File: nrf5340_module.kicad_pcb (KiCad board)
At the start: 4 copper layers, 18 x 40 mm, 42 parts, among them J1 U.FL_A-1JB, U1 nrf5340, Y1 32.768kHz, Y2 32MHz

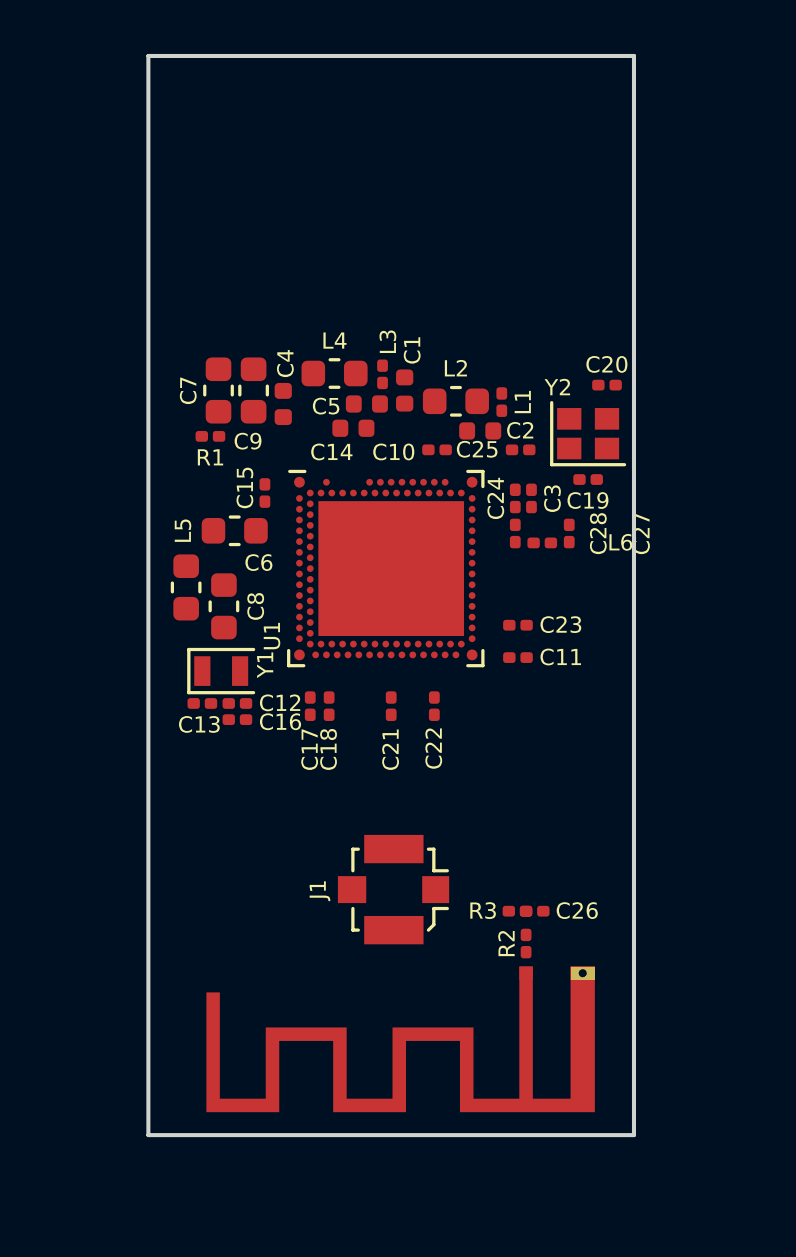
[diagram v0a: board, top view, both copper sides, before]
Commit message: first rev pcb without impedance matching
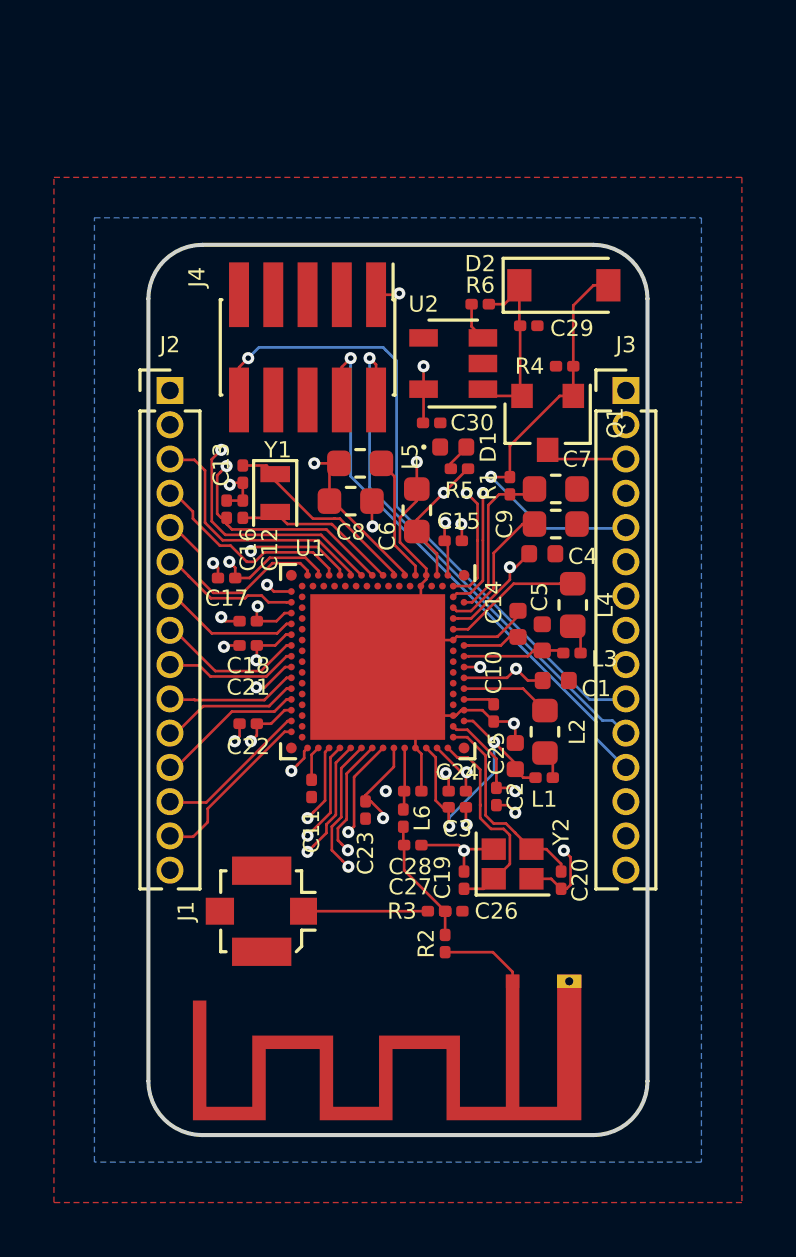
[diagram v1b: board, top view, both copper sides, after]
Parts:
- added C29: 10uF, Capacitor_SMD:C_0201_0603Metric, F.Cu at (234.1, 130.0)
- added C30: 10uF, Capacitor_SMD:C_0201_0603Metric, F.Cu at (230.5, 133.6)
- added D1: LED, LED_SMD:LED_0402_1005Metric, F.Cu at (231.3, 134.5)
- added D2: MBR120, Diode_SMD:D_SOD-123, F.Cu at (235.4, 128.5)
- added J2: Conn_01x15, Connector_PinHeader_1.27mm:PinHeader_1x15_P1.27mm_Vertical, F.Cu at (220.8, 132.4)
- added J3: Conn_01x15, Connector_PinHeader_1.27mm:PinHeader_1x15_P1.27mm_Vertical, F.Cu at (237.7, 132.4)
- added J4: Conn_ARM_JTAG_SWD_10, Connector_PinHeader_1.27mm:PinHeader_2x05_P1.27mm_Vertical_SMD, F.Cu at (225.9, 130.8)
- added Q1: Q_PMOS_GSD, Package_TO_SOT_SMD:SOT-23, F.Cu at (234.8, 133.6)
- added R4: 100k, Resistor_SMD:R_0201_0603Metric, F.Cu at (235.4, 131.5)
- added R5: 68R, Resistor_SMD:R_0201_0603Metric, F.Cu at (231.5, 135.3)
- added R6: 100k, Resistor_SMD:R_0201_0603Metric, F.Cu at (232.3, 129.2)
- added U2: AP2112K-3.3, Package_TO_SOT_SMD:SOT-23-5, F.Cu at (231.3, 131.4)
- moved C20 18.4 mm to (235.3, 150.6), turned to 90 degrees
- moved Y2 16.2 mm to (233.5, 149.9)
- moved C19 15.5 mm to (231.7, 150.6), turned to 270 degrees
- moved L1 14.0 mm to (234.7, 146.8), turned to 0 degrees
- moved C7 13.0 mm to (235.1, 136.1), turned to 0 degrees
- moved C27 12.9 mm to (229.8, 149.2), turned to 180 degrees
- moved C25 12.9 mm to (232.9, 147.4), turned to 90 degrees
- moved L2 12.7 mm to (234.7, 145.1), turned to 90 degrees
- moved L3 12.5 mm to (235.7, 142.1), turned to 0 degrees
- moved L4 12.3 mm to (235.7, 140.3), turned to 90 degrees
- moved C9 12.2 mm to (235.1, 137.3), turned to 0 degrees
- moved C1 12.1 mm to (235.1, 143.2), turned to 180 degrees
- moved C2 12.1 mm to (233.6, 145.9), turned to 90 degrees
- moved C3 11.8 mm to (231.4, 147.8), turned to 0 degrees
- moved L6 11.4 mm to (229.4, 148.2), turned to 90 degrees
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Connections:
- net P0.04 renamed Net-(U1-PadV2)
- net P0.05 renamed Net-(U1-PadY2)
- net P0.06 renamed Net-(U1-PadAB2)
- net P0.07 renamed Net-(U1-PadAD2)
- net P0.08 renamed Net-(U1-PadAH2)
- net P0.10 renamed Net-(U1-PadAK2)
- net P0.11 renamed Net-(U1-PadAK4)
- net P0.12 renamed Net-(U1-PadAK6)
- net P0.14 renamed Net-(U1-PadAK8)
- net P0.15 renamed Net-(U1-PadAK10)
- net P0.17 renamed Net-(U1-PadAK12)
- net P0.18 renamed Net-(U1-PadAK14)
- net P0.20 renamed Net-(U1-PadAK16)
- net P0.22 renamed Net-(U1-PadAK18)
- net P0.23 renamed Net-(U1-PadAK20)
- net P0.25 renamed Net-(U1-PadAK28)
- net P0.27 renamed Net-(U1-PadAK30)
- net P0.30 renamed Net-(U1-PadB24)
- net P0.31 renamed Net-(U1-PadB22)
- net P1.00 renamed Net-(U1-PadM2)
- net P1.01 renamed Net-(U1-PadP2)
- net P1.03 renamed Net-(U1-PadAF2)
- net P1.05 renamed Net-(U1-PadAK22)
- net P1.07 renamed Net-(U1-PadAK24)
- net P1.09 renamed Net-(U1-PadAK26)
- net P1.11 renamed Net-(U1-PadB20)
- net P1.12 renamed Net-(U1-PadB18)
- net P1.14 renamed Net-(U1-PadB16)
- net P1.15 renamed Net-(U1-PadB14)
- U1 pad B30: Net-(C12-Pad2) -> Net-(C20-Pad2)
- U1 pad C31: Net-(C13-Pad1) -> Net-(C19-Pad2)
- U1 pad K2: (no net) -> Net-(U1-PadK2)
- U1 pad N1: Net-(C19-Pad2) -> Net-(C13-Pad1)
- U1 pad R1: Net-(C20-Pad2) -> Net-(C12-Pad2)
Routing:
- net VDD_nRF: track 0.00 -> 60.5 mm, vias 0 -> 19
- net nRESET: track 0.00 -> 42.4 mm, vias 0 -> 2
- net GND: track 0.00 -> 41.9 mm, vias 0 -> 15
- net SWDCLK: track 0.00 -> 40.4 mm, vias 0 -> 2
- net SWDIO: track 0.00 -> 39.2 mm, vias 0 -> 2
- net P0.02: track 0.00 -> 24.9 mm, vias 0 -> 1
- net P0.28: track 0.00 -> 17.3 mm, vias 0 -> 1
- net P1.10: track 0.00 -> 16.2 mm, vias 0 -> 1
- net VBUS: track 0.00 -> 15.7 mm, vias 0 -> 1
- net P0.29: track 0.00 -> 15.0 mm, vias 0 -> 1
- net D+: track 0.00 -> 11.8 mm, vias 0 -> 1
- net D-: track 0.00 -> 11.0 mm, vias 0 -> 1
- net Net-(C2-Pad1): track 0.00 -> 10.8 mm, vias 0 -> 2
- net P0.03: track 0.00 -> 9.47 mm
- net Net-(C19-Pad2): track 0.00 -> 7.94 mm
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- added copper zone on F.Cu, net GND
- added copper zone on In1.Cu, net GND
- added copper zone on In2.Cu, net GND
- added copper zone on B.Cu, net VDD_nRF
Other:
- board size 18 x 40 mm -> 18.5 x 33 mm
- net class custom: clearance 0.145 -> 0.1; trace_width 0.145 -> 0.1
- rule trace_min: 0.145 -> 0.09

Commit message: fix traces underneath nrf gnd pad and VDD_HV
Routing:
- net P1.10: track 16.2 -> 14.4 mm
- net SWDIO: track 39.2 -> 38.4 mm

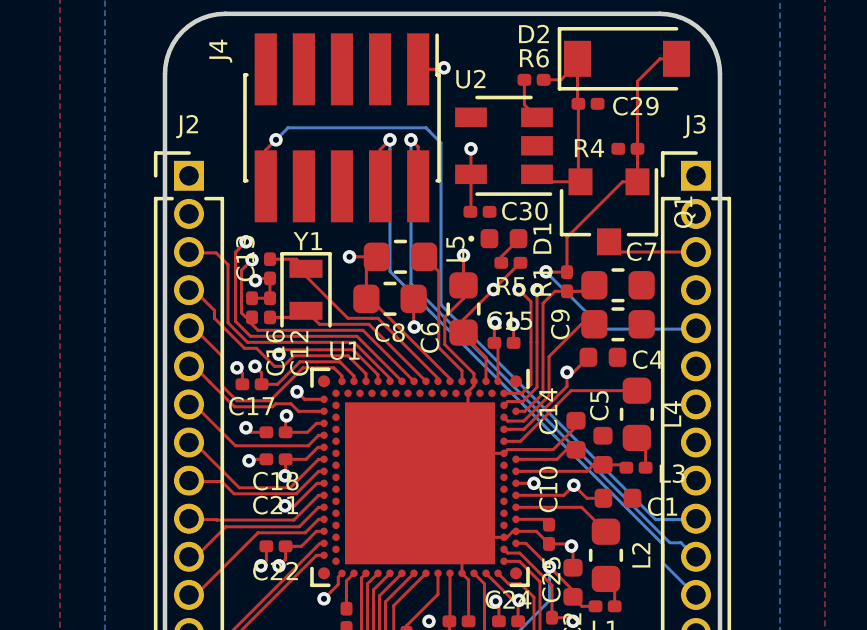
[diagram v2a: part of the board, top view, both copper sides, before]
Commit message: fix vdd_hv
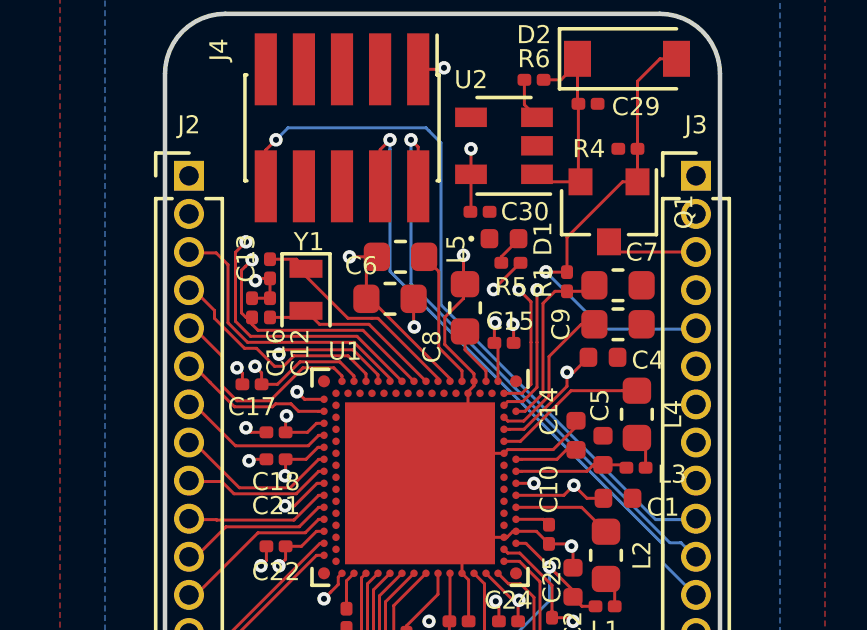
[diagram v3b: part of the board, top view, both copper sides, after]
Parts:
- moved C8 2.52 mm to (230.0, 136.8), turned to 90 degrees
- moved C6 2.47 mm to (227.5, 136.5), turned to 180 degrees
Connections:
- C8 pad 1: VDD_nRF -> VDD_HV
- J4 pad 6: Net-(J4-Pad6) -> (no net)
- J4 pad 7: Net-(J4-Pad7) -> (no net)
- J4 pad 8: Net-(J4-Pad8) -> (no net)
- U1 pad AB2: Net-(U1-PadAB2) -> (no net)
- U1 pad AD2: Net-(U1-PadAD2) -> (no net)
- U1 pad AF2: Net-(U1-PadAF2) -> (no net)
- U1 pad AH2: Net-(U1-PadAH2) -> (no net)
- U1 pad AK10: Net-(U1-PadAK10) -> (no net)
- U1 pad AK12: Net-(U1-PadAK12) -> (no net)
- U1 pad AK14: Net-(U1-PadAK14) -> (no net)
- U1 pad AK16: Net-(U1-PadAK16) -> (no net)
- U1 pad AK18: Net-(U1-PadAK18) -> (no net)
- U1 pad AK2: Net-(U1-PadAK2) -> (no net)
- U1 pad AK20: Net-(U1-PadAK20) -> (no net)
- U1 pad AK22: Net-(U1-PadAK22) -> (no net)
- U1 pad AK24: Net-(U1-PadAK24) -> (no net)
- U1 pad AK26: Net-(U1-PadAK26) -> (no net)
- U1 pad AK28: Net-(U1-PadAK28) -> (no net)
- U1 pad AK30: Net-(U1-PadAK30) -> (no net)
- U1 pad AK4: Net-(U1-PadAK4) -> (no net)
- U1 pad AK6: Net-(U1-PadAK6) -> (no net)
- U1 pad AK8: Net-(U1-PadAK8) -> (no net)
- U1 pad B14: Net-(U1-PadB14) -> (no net)
- U1 pad B16: Net-(U1-PadB16) -> (no net)
- U1 pad B18: Net-(U1-PadB18) -> (no net)
- U1 pad B20: Net-(U1-PadB20) -> (no net)
- U1 pad B22: Net-(U1-PadB22) -> (no net)
- U1 pad B24: Net-(U1-PadB24) -> (no net)
- U1 pad D2: Net-(U1-PadD2) -> (no net)
- U1 pad E1: VDD_nRF -> VDD_HV
- U1 pad F2: Net-(U1-PadF2) -> (no net)
- U1 pad K2: Net-(U1-PadK2) -> (no net)
- U1 pad M2: Net-(U1-PadM2) -> (no net)
- U1 pad P2: Net-(U1-PadP2) -> (no net)
- U1 pad T2: Net-(U1-PadT2) -> (no net)
- U1 pad V2: Net-(U1-PadV2) -> (no net)
- U1 pad Y2: Net-(U1-PadY2) -> (no net)
- U2 pad 4: Net-(U2-Pad4) -> (no net)
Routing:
- net VDD_nRF: track 60.5 -> 56.7 mm
- net VDD_HV: track 0.00 -> 1.95 mm
